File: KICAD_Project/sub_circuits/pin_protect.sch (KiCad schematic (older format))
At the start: 66 parts

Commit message: caps have been done with the scripts next up is the resistors.
Signed-off-by: Jared Harvey <TortiseGIT@jaredharvey.com>
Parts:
- C1301, C1302, C1303, C1304, C1305, C1306, C1307, C1308, C1309, C1310, C1311, C1312, C1313, C1314, C1315, C1316, C1317, C1318, C1319, C1320, C1321, C1322: Field3 -,- -> (none); Field4 -,- -> (none); Field5 50,V -> (none); Field6 10,% -> (none); Field7 Ceramic -> (none); Field8 other,more,stuff -> (none); V (none) -> 100V; construct (none) -> ceramic; mfg,# avx,08055F102K4Z2A -> (none); mfg,mfg# (none) -> avx,08051C104KAT2A; misc (none) -> other,more,stuff; tolerance (none) -> 10%; vend,# newark,26M5154 -> (none); vend1,vend1# (none) -> newark,96M1354

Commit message: Looks like the bulk components are golden now, there are still a couple straglers, mostly switch mode power supply stuff.
Signed-off-by: Jared Harvey <TortiseGIT@jaredharvey.com>
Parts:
- R1301, R1302, R1303, R1304, R1305, R1306, R1307, R1308, R1309, R1310, R1311, R1312, R1313, R1314, R1315, R1316, R1317, R1318, R1319, R1320, R1321, R1322: Field1 vishay,CRCW08051K00FKTA -> (none); Field2 newark,05F1507 -> (none); Field3 -,- -> (none); Field4 -,- -> (none); Field5 125,mW -> (none); Field6 1,% -> (none); Field7 thick film -> (none); Field8 other,more,stuff -> (none); construct (none) -> thick film; mfg,mfg# (none) -> vishay,CRCW08051K00FKTA; misc (none) -> other,more,stuff; tolerance (none) -> 1%; vend1,vend1# (none) -> newark,05F1507; w (none) -> 125mW

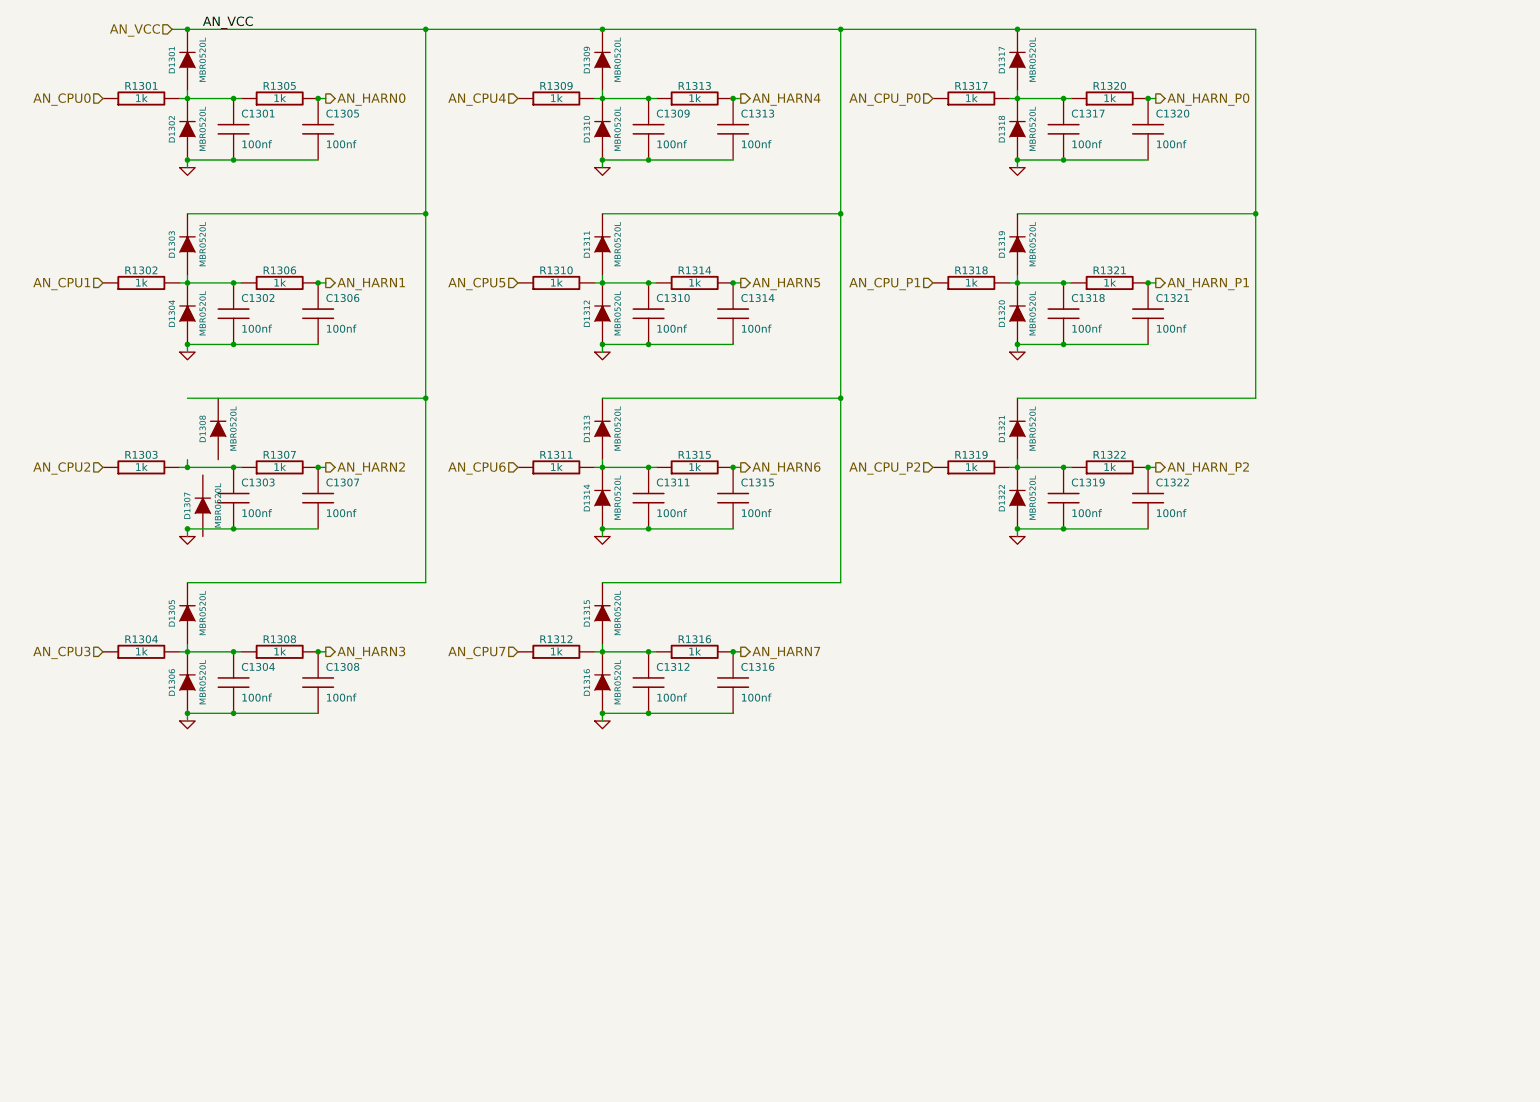
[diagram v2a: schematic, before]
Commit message: harness connector is much more ironed out now. CPU is not connected.
Signed-off-by: Jared Harvey <TortiseGIT@jaredharvey.com>
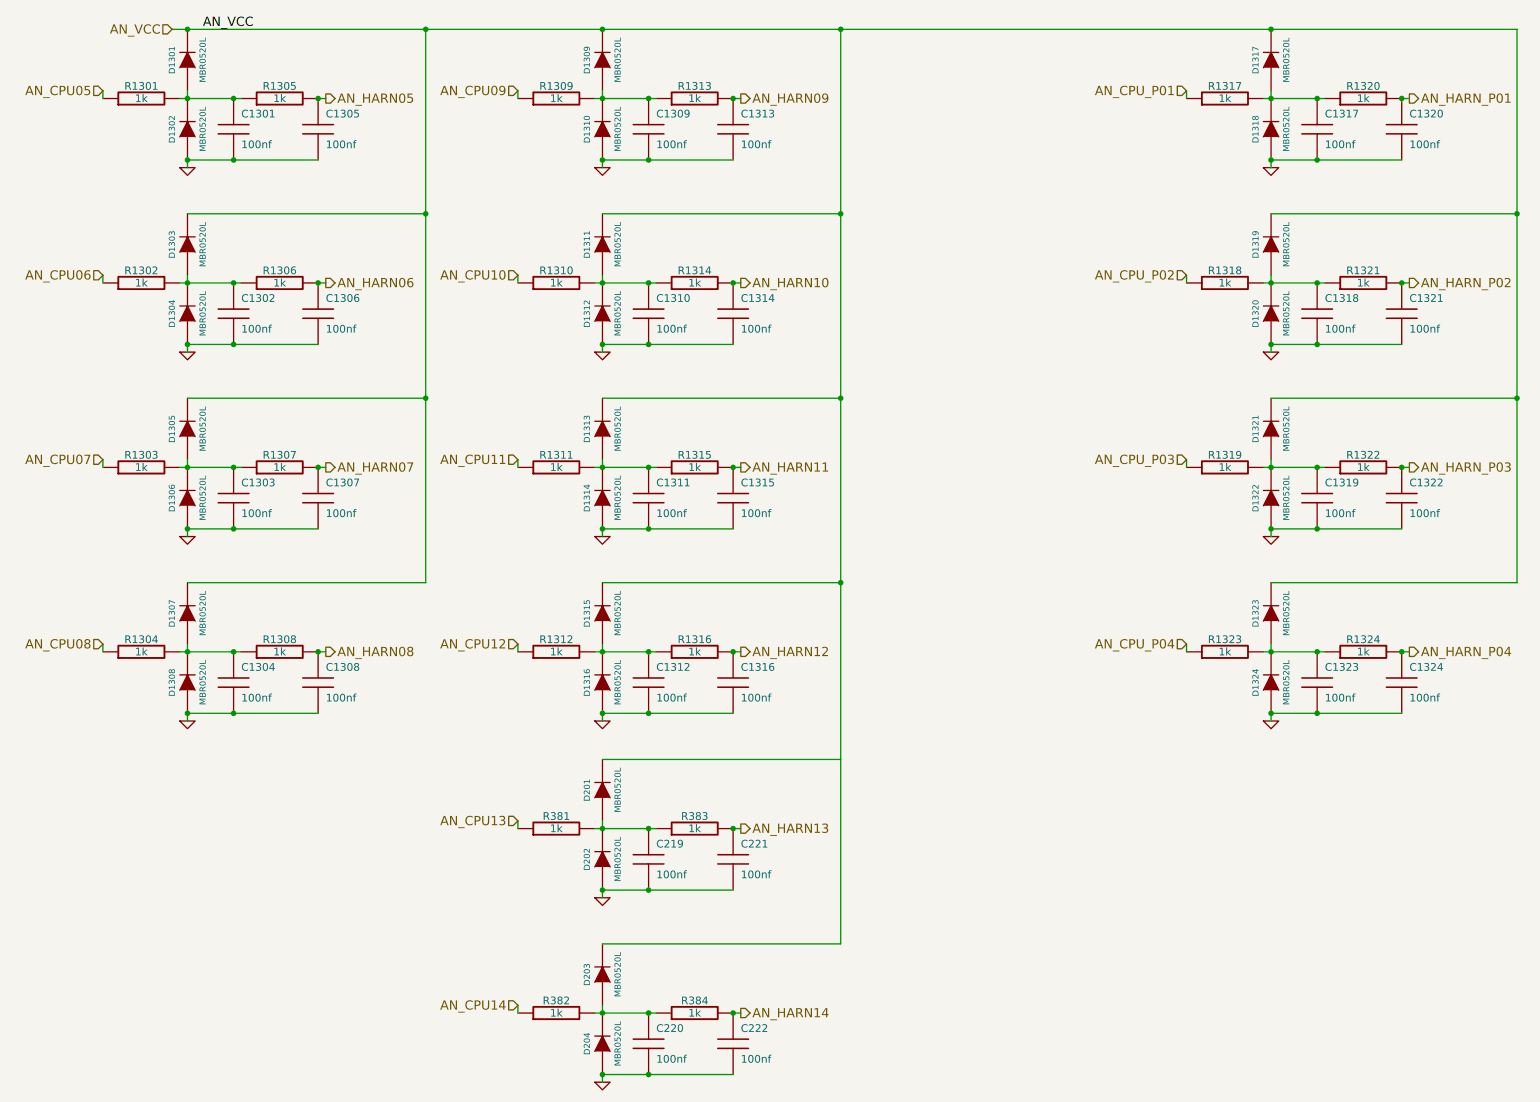
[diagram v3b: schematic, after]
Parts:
- added C1323, C1324, C219, C220, C221, C222: 100nf, SM0805-C1, symbol C
- added D1323, D1324, D201, D202, D203, D204: MBR0520L, SOD-123, symbol DIODE
- added R1323, R1324, R381, R382, R383, R384: 1k, SM0805, symbol R
- renumbered D1308 to D1305, D1307 to D1306, D1305 to D1307, D1306 to D1308
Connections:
- net AN_VCC: now also D1305.2 (K), D1323.2 (K), D203.2 (K)
- net GND: now also D1306.1 (A), C1323.2, C1324.2, C219.2, C220.2, C221.2, C222.2, D1324.1 (A), D202.1 (A), D204.1 (A)
- net at C1303.1, R1303.2, R1307.1: now also D1305.1 (A), D1306.2 (K)
- net AN_CPU0 renamed AN_CPU05
- net AN_CPU1 renamed AN_CPU06
- net AN_CPU2 renamed AN_CPU07
- net AN_CPU3 renamed AN_CPU08
- net AN_CPU4 renamed AN_CPU09
- net AN_CPU5 renamed AN_CPU10
- net AN_CPU6 renamed AN_CPU11
- net AN_CPU7 renamed AN_CPU12
- net AN_CPU_P0 renamed AN_CPU_P01
- net AN_CPU_P1 renamed AN_CPU_P02
- net AN_CPU_P2 renamed AN_CPU_P03
- net AN_HARN0 renamed AN_HARN05
- net AN_HARN1 renamed AN_HARN06
- net AN_HARN2 renamed AN_HARN07
- net AN_HARN3 renamed AN_HARN08
- net AN_HARN4 renamed AN_HARN09
- net AN_HARN5 renamed AN_HARN10
- net AN_HARN6 renamed AN_HARN11
- net AN_HARN7 renamed AN_HARN12
- net AN_HARN_P0 renamed AN_HARN_P01
- net AN_HARN_P1 renamed AN_HARN_P02
- net AN_HARN_P2 renamed AN_HARN_P03
- new net: C1323.1, D1323.1 (A), D1324.2 (K), R1323.2, R1324.1
- new net: C219.1, D201.1 (A), D202.2 (K), R381.2, R383.1
- new net: C220.1, D203.1 (A), D204.2 (K), R382.2, R384.1
- new net AN_CPU13: R381.1
- new net AN_CPU14: R382.1
- new net AN_CPU_P04: R1323.1
- new net AN_HARN13: C221.1, R383.2
- new net AN_HARN14: C222.1, R384.2
- new net AN_HARN_P04: C1324.1, R1324.2
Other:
- moved on the sheet: C1317, C1318, C1319, C1320, C1321, C1322, D1305, D1306, D1317, D1318, D1319, D1320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

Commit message: several pins on the SOM are now connected.
Signed-off-by: Jared Harvey <TortiseGIT@jaredharvey.com>
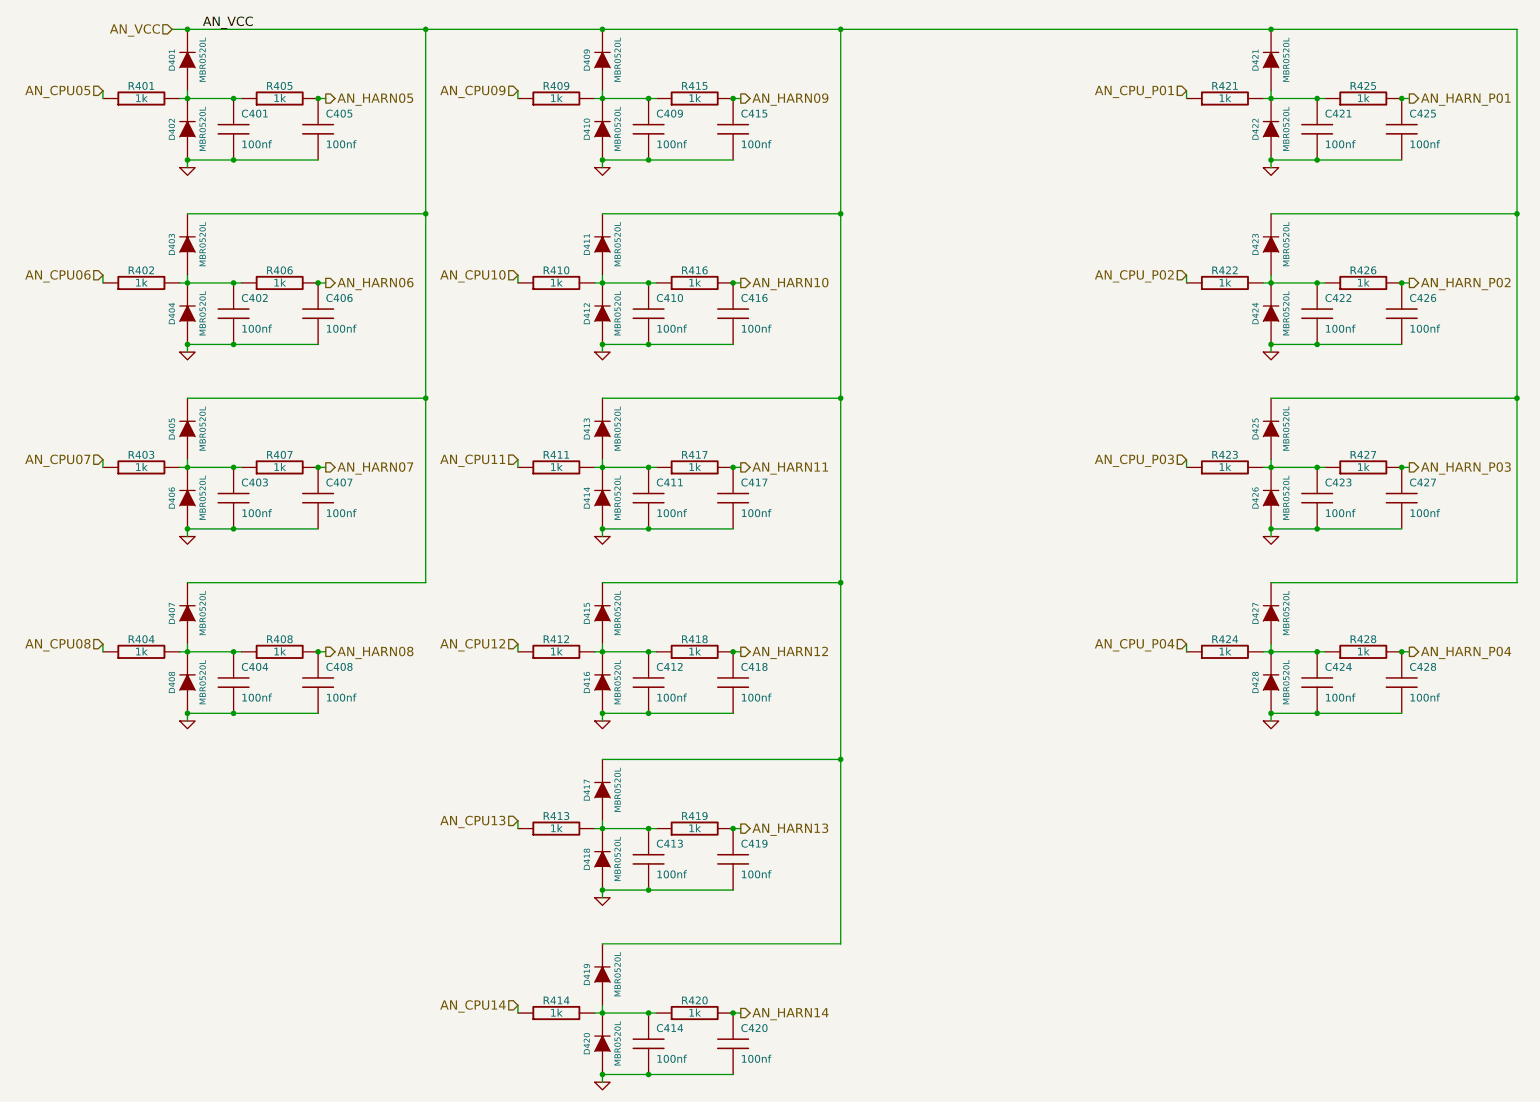
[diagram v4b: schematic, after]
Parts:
- renumbered C1301 to C401, C1302 to C402, C1303 to C403, C1304 to C404, C1305 to C405, C1306 to C406, C1307 to C407, C1308 to C408, C1309 to C409, C1310 to C410, C1311 to C411, C1312 to C412, C219 to C413, C220 to C414, C1313 to C415, C1314 to C416, C1315 to C417, C1316 to C418, C221 to C419, C222 to C420, C1317 to C421, C1318 to C422, C1319 to C423, C1323 to C424, C1320 to C425, C1321 to C426, C1322 to C427, C1324 to C428, D1301 to D401, D1302 to D402, D1303 to D403, D1304 to D404, D1305 to D405, D1306 to D406, D1307 to D407, D1308 to D408, D1309 to D409, D1310 to D410, D1311 to D411, D1312 to D412, D1313 to D413, D1314 to D414, D1315 to D415, D1316 to D416, D201 to D417, D202 to D418, D203 to D419, D204 to D420, D1317 to D421, D1318 to D422, D1319 to D423, D1320 to D424, D1321 to D425, D1322 to D426, D1323 to D427, D1324 to D428, R1301 to R401, R1302 to R402, R1303 to R403, R1304 to R404, R1305 to R405, R1306 to R406, R1307 to R407, R1308 to R408, R1309 to R409, R1310 to R410, R1311 to R411, R1312 to R412, R381 to R413, R382 to R414, R1313 to R415, R1314 to R416, R1315 to R417, R1316 to R418, R383 to R419, R384 to R420, R1317 to R421, R1318 to R422, R1319 to R423, R1323 to R424, R1320 to R425, R1321 to R426, R1322 to R427, R1324 to R428
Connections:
- net AN_VCC: now also D417.2 (K)
